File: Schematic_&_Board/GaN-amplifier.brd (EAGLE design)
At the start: 77 parts, among them IC1 LT3080, Q1 MMBT3906LT1SMD, T1 IRL3714S, T2 IRL3714S, T3 IRL3714S, T4 IRL3714S, T5 BSP89, U1 TPS7A30XX, U2 HMC1099, U3 LT1783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

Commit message: Started board layout
Moved all the components so they fit in the allowed area. Need to
detangle air wires next.

DSB
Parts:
- moved C23 609.9 mm to (41.9, 27.9)
- moved C24 609.9 mm to (41.9, 24.1)
- moved C25 609.9 mm to (41.9, 20.3)
- moved C26 609.9 mm to (41.9, 16.5)
- moved L2 609.9 mm to (41.9, 12.7)
- moved L3 609.9 mm to (34.3, 16.5)
- moved X3 609.9 mm to (59.7, 57.1)
- moved R29 609.9 mm to (43.2, 34.3)
- moved R28 581.1 mm to (83.8, 36.8), turned to 90 degrees
- moved R27 576.3 mm to (80.0, 36.8), turned to 90 degrees
- moved R26 571.5 mm to (76.2, 36.8), turned to 90 degrees
- moved R25 566.7 mm to (72.4, 36.8), turned to 90 degrees
- moved C22 561.9 mm to (68.6, 36.8), turned to 90 degrees
- moved T5 554.9 mm to (61.0, 40.6), turned to 90 degrees
- moved U5 545.3 mm to (54.6, 38.1), turned to 90 degrees
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
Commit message: Parts positioned
I've positioned the components. Now routing needs to happen.

DSB
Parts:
- added JP3: (no value), pinhead:1X03
- moved IC1 137.0 mm to (15.2, 39.4), turned to 180 degrees
- moved T2 125.2 mm to (10.2, 17.8)
- moved R10 124.6 mm to (25.4, 10.2), turned to 180 degrees
- moved R12 123.7 mm to (34.3, 16.5), turned to 0 degrees
- moved R11 121.0 mm to (33.0, 14.0)
- moved R7 118.2 mm to (15.2, 27.9), turned to 270 degrees
- moved C18 117.4 mm to (29.2, 17.8), turned to 180 degrees
- moved C10 117.1 mm to (5.08, 26.7), turned to 0 degrees
- moved R6 114.8 mm to (15.2, 25.4), turned to 270 degrees
- moved R9 114.6 mm to (24.1, 12.7), turned to 0 degrees
- moved R5 112.6 mm to (22.9, 19.1)
- moved C11 112.3 mm to (14.0, 25.4)
- moved C17 112.0 mm to (30.5, 14.0)
- moved C9 110.5 mm to (6.35, 30.5), turned to 0 degrees
- moved Q1 104.5 mm to (24.1, 15.2)
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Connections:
- removed net N$32: L3.P$2, R29.P$3
- new net VL: R26.P$2, R29.P$2
- net +24V: now also JP3.1
- net -24V: now also JP3.3
- net GND: now also JP3.2
- net N$23: now also L3.P$2, R29.P$4; no longer R26.P$2, R29.P$1
- net N$27: now also R29.P$1; no longer R29.P$2
- net VDD: now also R29.P$3; no longer R29.P$4
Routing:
- added copper zone on layer 1, net GND
- added copper zone on layer 16, net GND
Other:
- board outline added: 120.7 x 50.8 mm

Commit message: Few adjustments
Rearranged the board to be a bit more compact.

DSB
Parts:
- moved JP1 15.7 mm to (64.8, 10.2)
- moved C14 14.5 mm to (53.3, 3.81)
- moved C15 14.5 mm to (53.3, 6.35)
- moved C16 14.5 mm to (55.9, 6.35)
- moved U6 14.5 mm to (54.6, 12.7)
- moved R2 14.5 mm to (50.8, 6.35)
- moved R3 14.5 mm to (49.5, 3.81)
- moved R4 14.5 mm to (58.4, 7.62)
- moved T2 14.4 mm to (20.3, 7.62)
- moved C18 13.1 mm to (40.6, 11.4)
- moved Q1 13.1 mm to (35.6, 8.89)
- moved R10 13.1 mm to (36.8, 3.81)
- moved R11 13.1 mm to (44.5, 7.62)
- moved R12 13.1 mm to (45.7, 10.2)
- moved R5 13.1 mm to (34.3, 12.7)
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
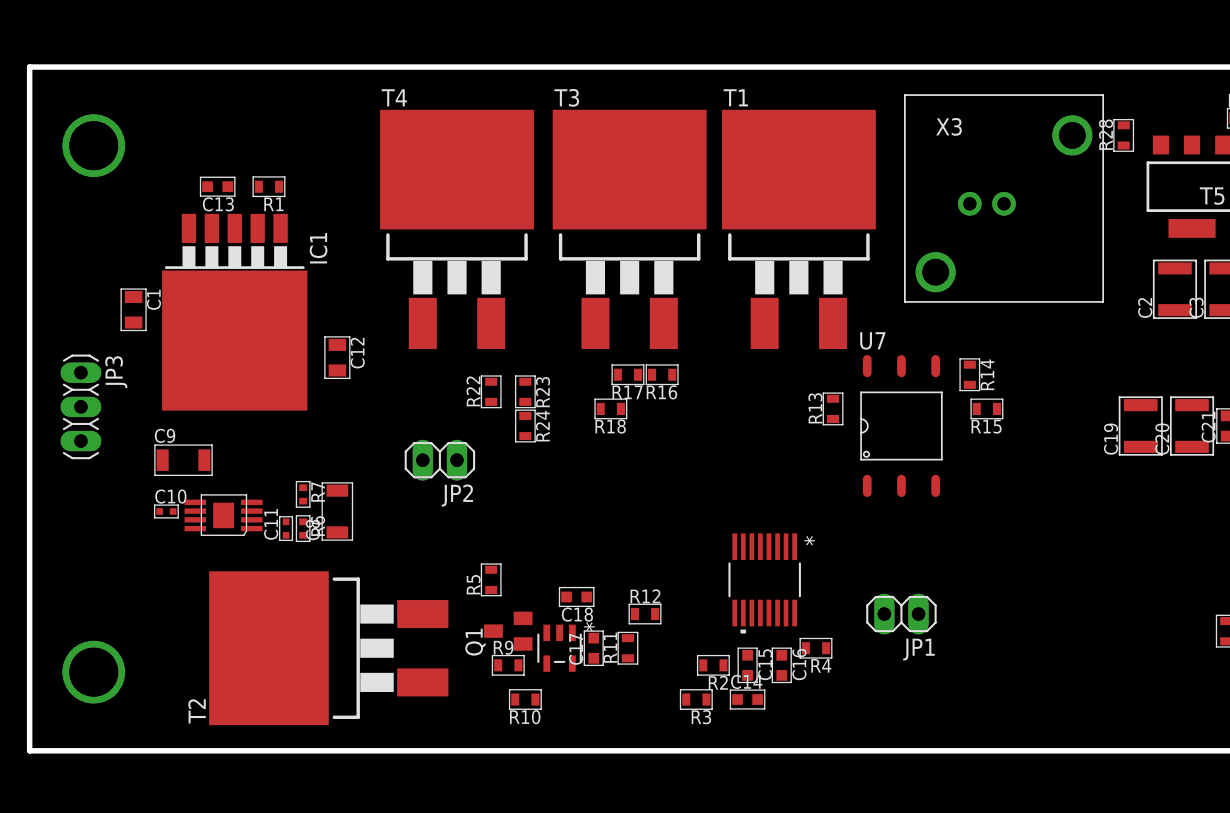
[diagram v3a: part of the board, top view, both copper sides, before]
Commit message: Power Sequencing Layed Out
I've finished routing the power sequencing part of the PCB. Need to copy
positions of RF components from eval board gerber and design 50 Ohm
striplines.

DSB
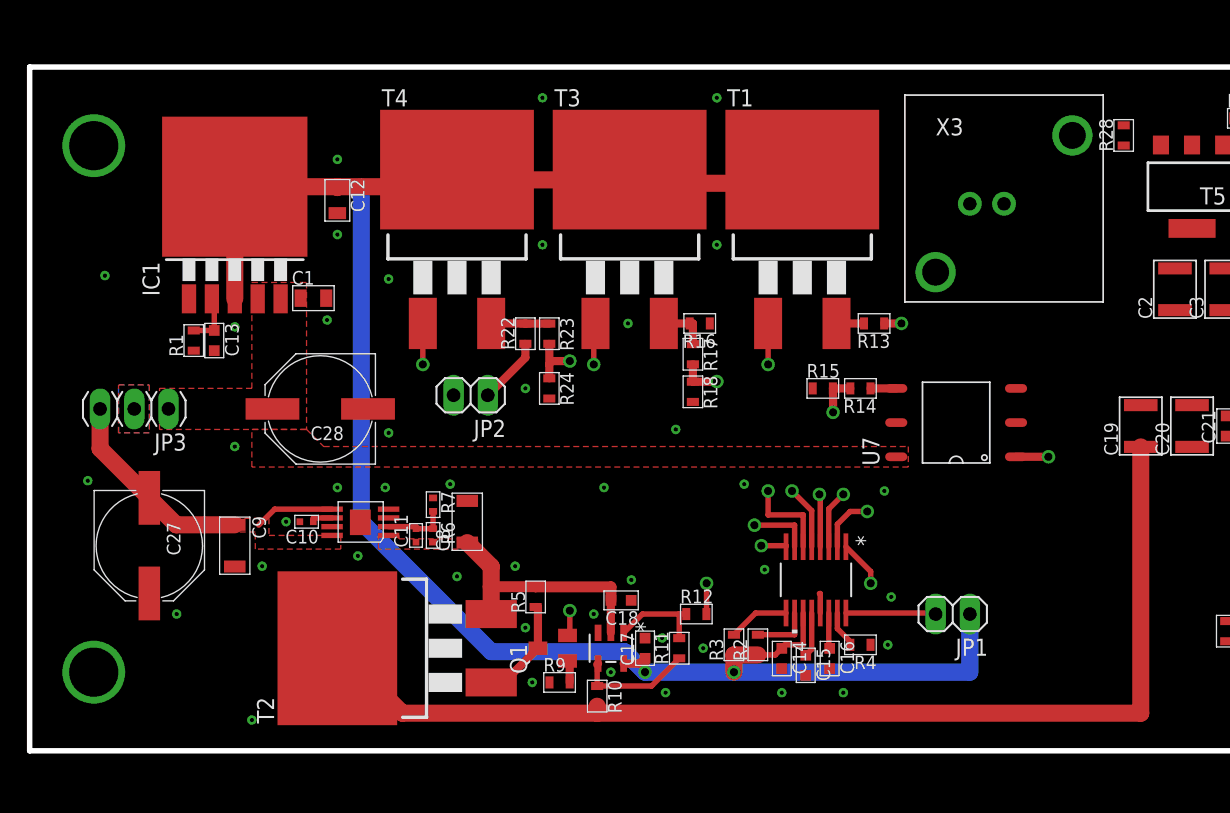
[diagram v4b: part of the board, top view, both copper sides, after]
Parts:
- added C27, C28: 220u, jqi_passives:PANASONIC_F
- moved C1 13.4 mm to (21.1, 33.6), turned to 0 degrees
- moved R1 12.7 mm to (12.2, 30.5), turned to 90 degrees
- moved R15 12.3 mm to (58.9, 26.9), turned to 0 degrees
- moved C12 11.7 mm to (22.9, 40.9)
- moved C13 11.4 mm to (13.7, 30.5), turned to 270 degrees
- moved C10 10.4 mm to (20.6, 17.0), turned to 180 degrees
- moved U1 10.2 mm to (26.7, 16.0)
- moved C8 9.68 mm to (32.5, 17.0)
- moved R7 9.68 mm to (30.0, 18.3)
- moved C11 9.67 mm to (28.7, 16.0)
- moved R6 9.67 mm to (30.0, 16.0)
- moved R14 8.19 mm to (61.7, 26.9), turned to 180 degrees
- moved C9 7.41 mm to (15.2, 15.2), turned to 270 degrees
- moved R13 7.04 mm to (62.7, 31.8), turned to 180 degrees
- moved IC1 6.35 mm to (15.2, 39.4), turned to 0 degrees
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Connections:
- net +24V: now also C28.+
- net -24V: now also C27.-
- net GND: now also C27.+, C28.-
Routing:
- net +5V: track 0.00 -> 142.0 mm, vias 0 -> 2
- net -8V: track 0.00 -> 82.0 mm
- net RF_EN: track 0.00 -> 38.2 mm, vias 0 -> 2
- net RF_DET: track 0.00 -> 32.4 mm, vias 0 -> 2
- net VPIN_EN: track 0.00 -> 31.5 mm, vias 0 -> 2
- net VGG_EN: track 0.00 -> 24.6 mm, vias 0 -> 2
- net -24V: track 0.00 -> 21.2 mm
- net VGG_DET: track 0.00 -> 20.3 mm, vias 0 -> 2
- net VDD_EN: track 0.00 -> 19.2 mm, vias 0 -> 2
- net N$13: track 0.00 -> 18.7 mm, vias 0 -> 2
- net AMP_POW: track 0.00 -> 18.4 mm
- net VPIN_DET: track 0.00 -> 18.0 mm, vias 0 -> 2
- net VDD_DET: track 0.00 -> 15.8 mm, vias 0 -> 2
- net N$12: track 0.00 -> 8.64 mm
- net N$9: track 0.00 -> 7.75 mm
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- added copper zone on layer 1, net +24V
- added copper zone on layer 1, net -24V
- added copper zone on layer 1, net AMP_POW

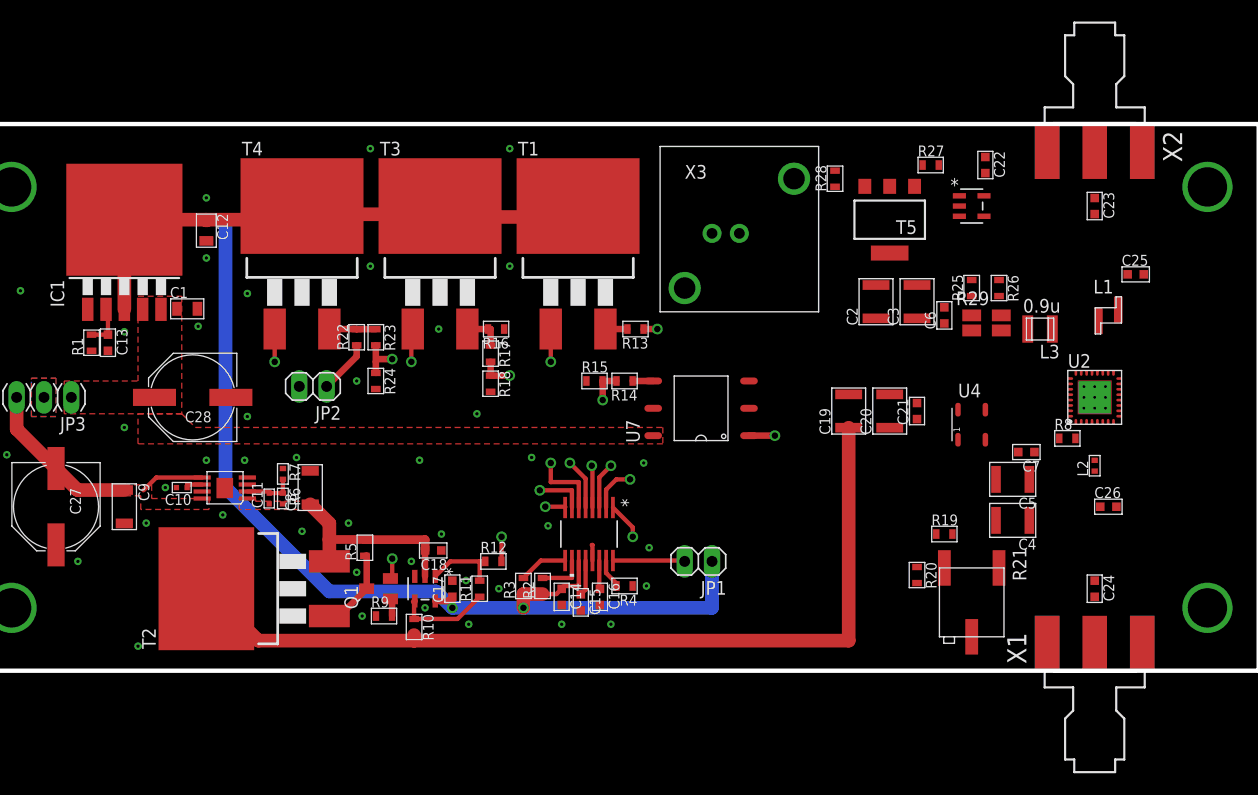
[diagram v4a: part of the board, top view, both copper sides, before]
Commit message: Add VGG Buffer
Added buffer for the GaN amp gate voltage. Also made progress on RF
layout.

DSB
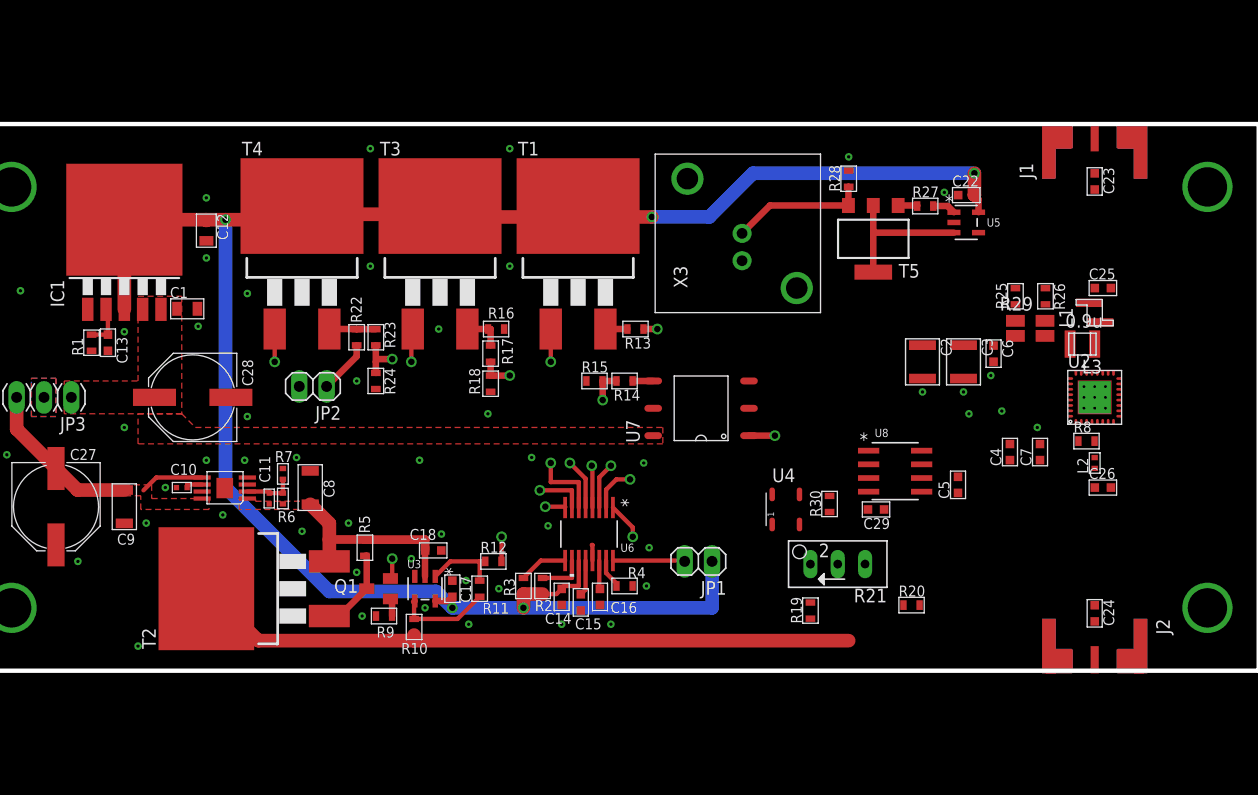
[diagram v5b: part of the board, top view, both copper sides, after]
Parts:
- removed C19, C20: 10u, jqi_passives:C_MLCC_1210
- removed C21: 2.2n, jqi_passives:C_MLCC_0603
- removed X1, X2: SMA-142-0701-801/806, con-coax:J502-ND-142-0701-801/806
- added C29: 100n, jqi_passives:C_MLCC_0603
- added J1, J2: JOHNSON_SMA_EDGE_LAUNCH_142-0701-851, connector-jqi:JOHNSON_SMA_EDGE_LAUNCH_142-0701-851
- added R30: 50, jqi_passives:R_0603
- added U8: LTC1152IS8TRPBF, linear-technology-jqi:SO-8_S
- C15: value 150n -> 200n
- C16: value 200n -> 150n
- C4: value 10u -> 1u; device jqi_passives:C_MLCC_1210 -> jqi_passives:C_MLCC_0603
- C5: value 10u -> 1n; device jqi_passives:C_MLCC_1210 -> jqi_passives:C_MLCC_0603
- R19: value 200 -> 2k
- R20: value 100 -> 1k
- R21: value 500 -> 5k; device rlc-jqi:3269P -> jqi_passives:RJ24
- moved U4 19.0 mm to (76.7, 15.0)
- moved R19 14.3 mm to (79.0, 5.59), turned to 90 degrees
- moved R21 12.9 mm to (81.5, 9.91), turned to 180 degrees
- moved C2 7.06 mm to (89.4, 28.7), turned to 270 degrees
- moved C3 7.06 mm to (93.2, 28.7), turned to 270 degrees
- moved C4 6.36 mm to (97.5, 20.3), turned to 90 degrees
- moved C6 5.79 mm to (96.0, 29.5), turned to 270 degrees
- moved C5 5.11 mm to (92.7, 17.3), turned to 90 degrees
- moved R26 4.38 mm to (100.8, 34.8)
- moved L3 4.18 mm to (104.3, 30.4)
- moved R25 4.13 mm to (98.0, 34.8)
- moved R29 4.10 mm to (98.0, 32.5)
- moved R27 3.84 mm to (89.7, 43.2)
- moved C22 3.31 mm to (93.5, 44.2), turned to 0 degrees
- moved C25 3.30 mm to (106.2, 35.6)
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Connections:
- removed net N$18: C4.P$1, C5.P$1, C7.P$1, R21.2, R8.P$1
- new net N$32: C5.P$1, U8.5
- new net N$36: R21.2, R30.P$1
- new net VGG: C4.P$1, C5.P$2, C7.P$1, R8.P$1, U8.2, U8.6
- new net V_GATE: L2.P$2, R8.P$2, U2.4, U2.5
- net -8V: no longer C19.P$1, C20.P$1, C21.P$1
- net AMP_POW: now also C29.P$2, U8.4
- net GND: now also C29.P$1, J1.P$2, J1.P$3, J1.P$4, J1.P$5, J2.P$2, J2.P$3, J2.P$4, J2.P$5, U8.7; no longer C19.P$2, C20.P$2, C21.P$2, C5.P$2, X1.G@1, X1.G@2, X1.G@3, X1.G@4, X2.G@1, X2.G@2, X2.G@3, X2.G@4
- net N$19: now also R21.1; no longer R21.3
- net N$20: now also R21.3; no longer R21.1
- net N$30: now also J1.P$1; no longer X2.1
- net N$31: now also J2.P$1; no longer X1.1
- net V_PINCH: now also R30.P$2, U8.3; no longer L2.P$2, R8.P$2, U2.4, U2.5
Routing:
- net +5V: track 142.0 -> 185.2 mm, vias 2 -> 5
- net -8V: track 82.0 -> 62.2 mm
- net N$24: track 0.00 -> 13.7 mm
- net N$28: track 0.00 -> 12.7 mm
- net N$25: track 0.00 -> 2.15 mm
- net N$26: track 0.00 -> 1.82 mm
- net GND: vias 46 -> 54

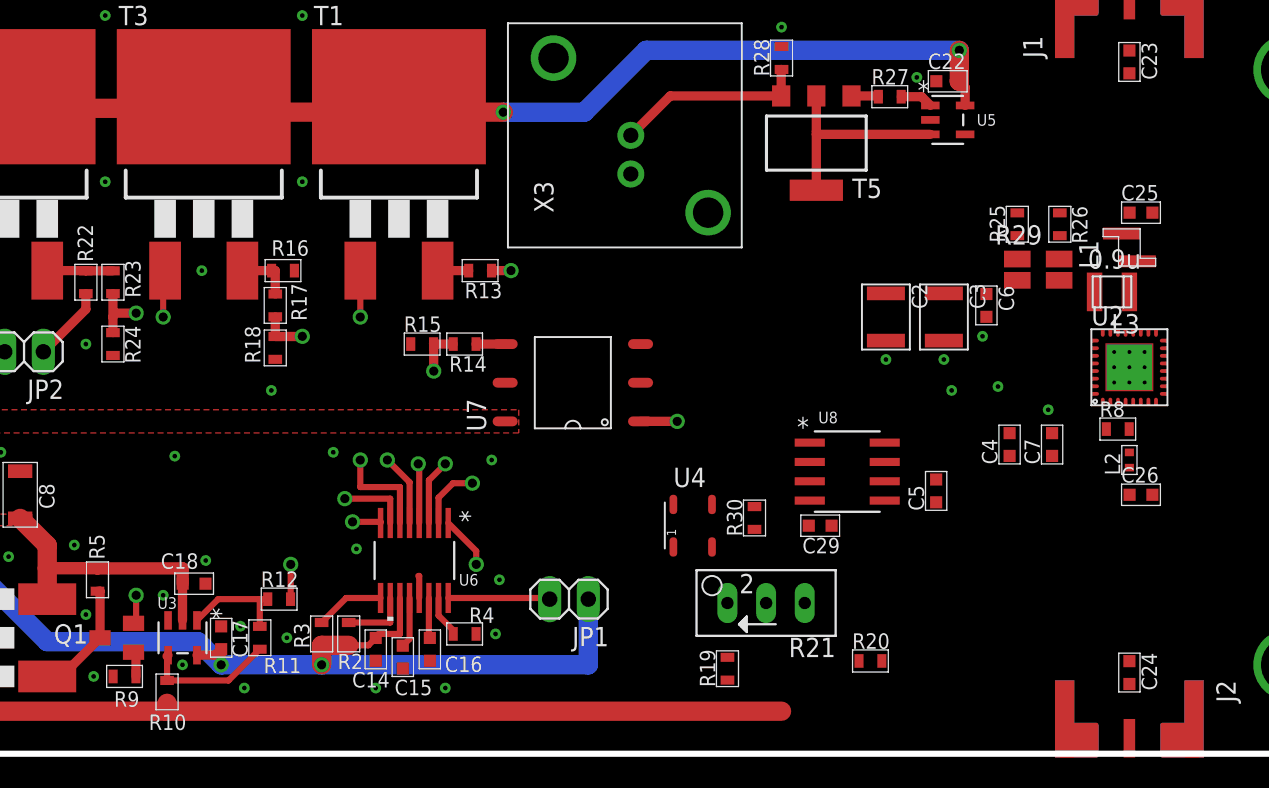
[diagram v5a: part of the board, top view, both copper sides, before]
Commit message: Routed Buffer
I’ve routed the gate bias buffer part of the circuit. The only thing
that’s left is routing the RF traces.

DSB
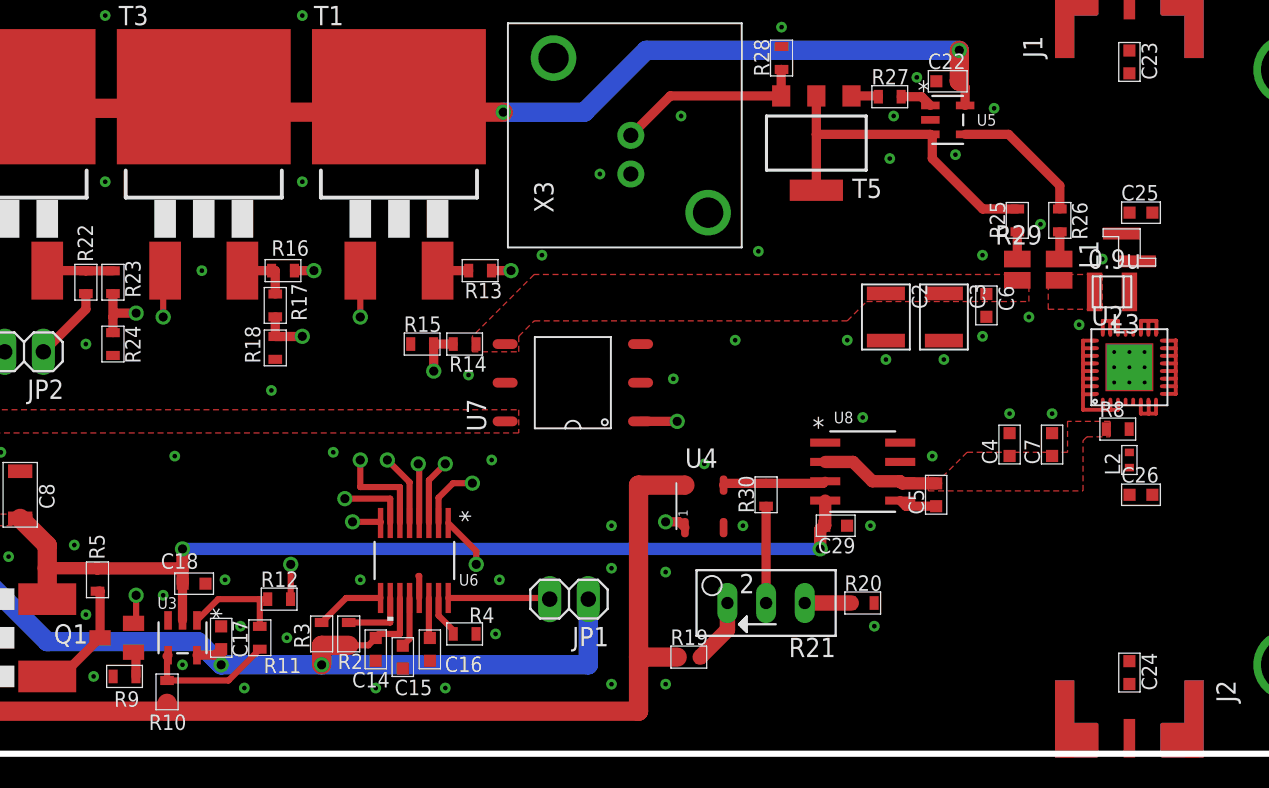
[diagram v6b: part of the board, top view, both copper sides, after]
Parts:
- moved R20 3.84 mm to (87.9, 9.91)
- moved R19 2.65 mm to (76.5, 6.35), turned to 0 degrees
- moved R30 1.70 mm to (81.5, 17.0)
- moved U4 1.48 mm to (77.5, 16.3)
- moved U8 1.02 mm to (87.9, 18.5)
- moved C29 1.02 mm to (86.1, 15.0)
- moved C5 0.25 mm to (92.7, 17.0)
- moved R25 0.25 mm to (98.0, 35.1)
- moved R26 0.25 mm to (100.8, 35.1)
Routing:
- net AMP_POW: track 18.4 -> 64.9 mm, vias 0 -> 2
- net GND: track 1.51 -> 36.6 mm, vias 54 -> 81
- net N$16: track 0.00 -> 32.7 mm, vias 0 -> 2
- net -8V: track 62.2 -> 73.3 mm
- net N$29: track 0.00 -> 9.15 mm
- net N$24: track 13.7 -> 22.3 mm
- net VGG: track 0.00 -> 7.87 mm
- net V_PINCH: track 0.00 -> 6.79 mm
- net N$36: track 0.00 -> 6.36 mm
- net N$19: track 0.00 -> 4.30 mm
- net N$20: track 0.00 -> 3.06 mm
- net N$32: track 0.00 -> 2.52 mm
- net VDD: track 1.91 -> 0.00 mm
- net VL: track 0.00 -> 1.81 mm
- net N$27: track 0.00 -> 1.79 mm
- added copper zone on layer 2, net GND
- added copper zone on layer 1, net N$23
- added copper zone on layer 1, net VDD
- added copper zone on layer 1, net VGG
